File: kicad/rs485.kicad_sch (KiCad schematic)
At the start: 12 parts

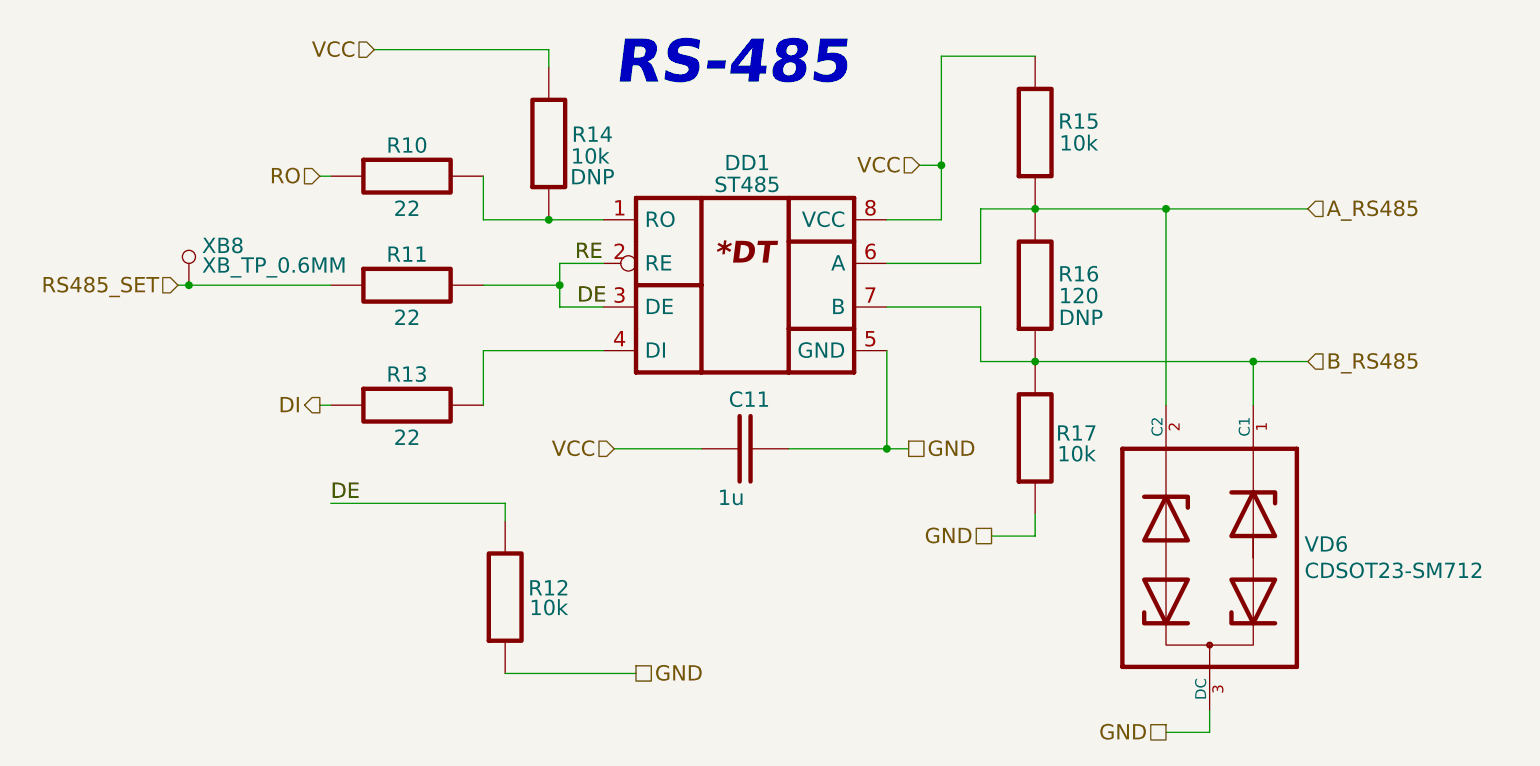
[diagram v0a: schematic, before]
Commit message: Reannotate schematic; Fix 5032 crystal footprint field; Update PCB with 5032 crystal
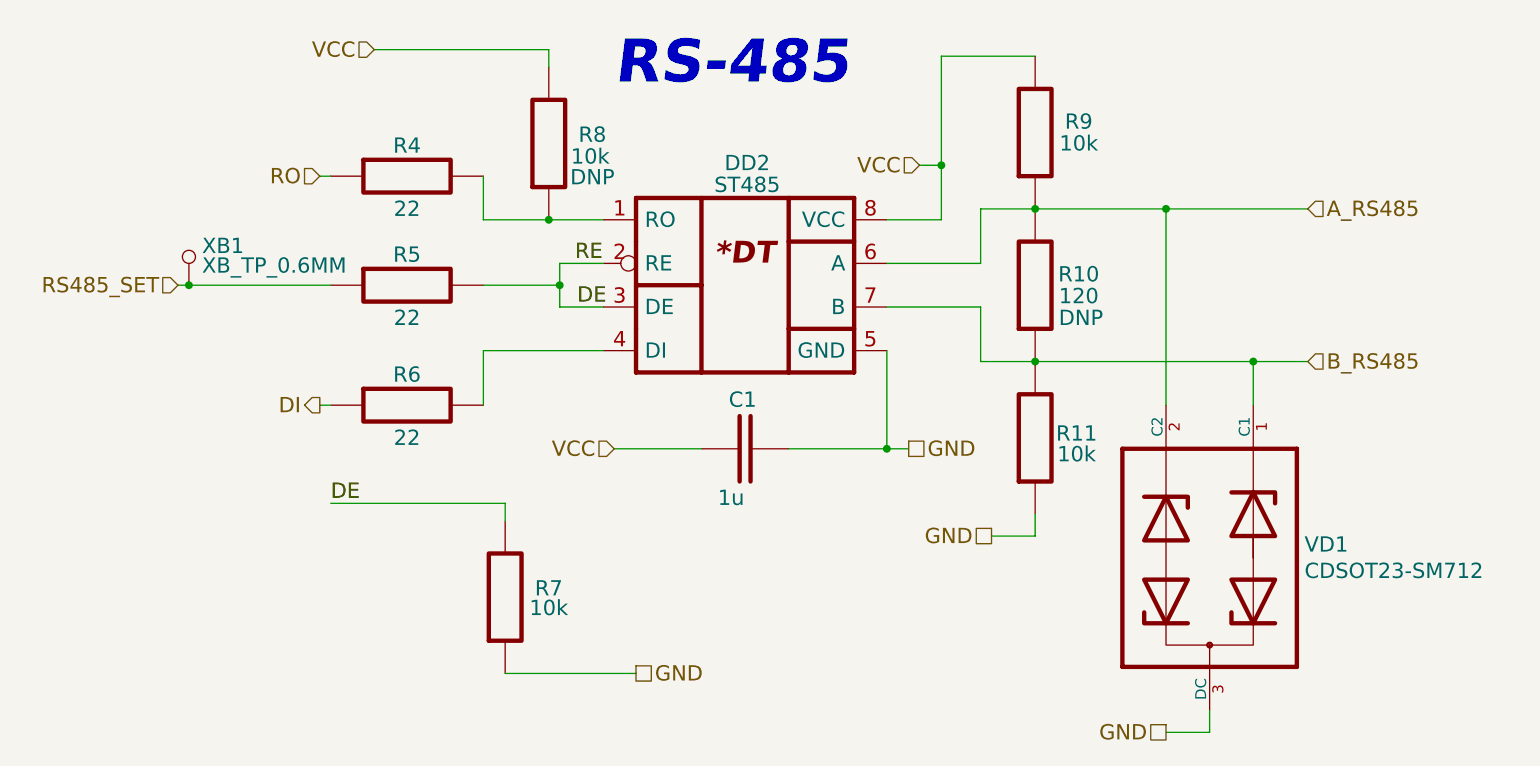
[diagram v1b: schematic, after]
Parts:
- renumbered C11 to C1, DD1 to DD2, R16 to R10, R17 to R11, R10 to R4, R11 to R5, R13 to R6, R12 to R7, R14 to R8, R15 to R9, VD6 to VD1, XB8 to XB1
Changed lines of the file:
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@@
   (symbol (lib_id "Resistors:R_RES") (at 179.578 86.36 90) (unit 1)
     (in_bom yes) (on_board yes)
-    (property "Reference" "R16" (id 0) (at 184.658 85.09 90)
+    (property "Reference" "R10" (id 0) (at 184.658 85.09 90)
       (effects (font (size 1.778 1.778)))
     )
@@
   (symbol (lib_id "Diodes:VD_TVS_ARRAY4") (at 204.978 118.11 270) (unit 1)
     (in_bom yes) (on_board yes)
-    (property "Reference" "VD6" (id 0) (at 210.947 116.5606 90)
+    (property "Reference" "VD1" (id 0) (at 210.947 116.5606 90)
       (effects (font (size 1.778 1.778)) (justify left))
     )
@@
   (symbol (lib_id "Capacitors:C_CAP") (at 145.796 105.41 0) (unit 1)
     (in_bom yes) (on_board yes)
-    (property "Reference" "C11" (id 0) (at 143.891 99.695 0)
+    (property "Reference" "C1" (id 0) (at 143.891 99.695 0)
       (effects (font (size 1.778 1.778)) (justify left))
     )
@@
   (symbol (lib_id "Chips:ST485") (at 145.796 86.36 0) (unit 1)
     (in_bom yes) (on_board yes)
-    (property "Reference" "DD1" (id 0) (at 146.05 72.136 0)
+    (property "Reference" "DD2" (id 0) (at 146.05 72.136 0)
       (effects (font (size 1.778 1.778)))
     )
@@
   (symbol (lib_id "Resistors:R_RES") (at 106.426 86.36 0) (unit 1)
     (in_bom yes) (on_board yes)
-    (property "Reference" "R11" (id 0) (at 106.426 82.804 0)
+    (property "Reference" "R5" (id 0) (at 106.426 82.804 0)
       (effects (font (size 1.778 1.778)))
     )
@@
   (symbol (lib_id "Resistors:R_RES") (at 106.426 73.66 0) (unit 1)
     (in_bom yes) (on_board yes)
-    (property "Reference" "R10" (id 0) (at 106.426 70.104 0)
+    (property "Reference" "R4" (id 0) (at 106.426 70.104 0)
       (effects (font (size 1.778 1.778)))
     )
@@
   (symbol (lib_id "Resistors:R_RES") (at 179.578 104.14 90) (unit 1)
     (in_bom yes) (on_board yes)
-    (property "Reference" "R17" (id 0) (at 184.404 103.632 90)
+    (property "Reference" "R11" (id 0) (at 184.404 103.632 90)
       (effects (font (size 1.778 1.778)))
     )
@@
   (symbol (lib_id "Resistors:R_RES") (at 122.936 69.85 90) (unit 1)
     (in_bom yes) (on_board yes)
-    (property "Reference" "R14" (id 0) (at 128.016 68.834 90)
+    (property "Reference" "R8" (id 0) (at 128.016 68.834 90)
       (effects (font (size 1.778 1.778)))
     )
@@
   (symbol (lib_id "Resistors:R_RES") (at 106.426 100.33 0) (unit 1)
     (in_bom yes) (on_board yes)
-    (property "Reference" "R13" (id 0) (at 106.426 96.774 0)
+    (property "Reference" "R6" (id 0) (at 106.426 96.774 0)
       (effects (font (size 1.778 1.778)))
     )
@@
   (symbol (lib_id "Resistors:R_RES") (at 117.856 122.6819 90) (unit 1)
     (in_bom yes) (on_board yes)
-    (property "Reference" "R12" (id 0) (at 122.936 121.6659 90)
+    (property "Reference" "R7" (id 0) (at 122.936 121.6659 90)
       (effects (font (size 1.778 1.778)))
     )
@@
   (symbol (lib_id "Connectors:XB_TP_0.6MM") (at 81.026 86.36 0) (unit 1)
     (in_bom no) (on_board yes)
-    (property "Reference" "XB8" (id 0) (at 82.55 81.788 0)
+    (property "Reference" "XB1" (id 0) (at 82.55 81.788 0)
       (effects (font (size 1.778 1.778)) (justify left))
     )
@@
   (symbol (lib_id "Resistors:R_RES") (at 179.578 68.58 90) (unit 1)
     (in_bom yes) (on_board yes)
-    (property "Reference" "R15" (id 0) (at 184.658 67.31 90)
-      (effects (font (size 1.778 1.778)))
-    )
+    (property "Reference" "R9" (id 0) (at 184.658 67.31 90)
+      (effects (font (size 1.778 1.778)))
+    )

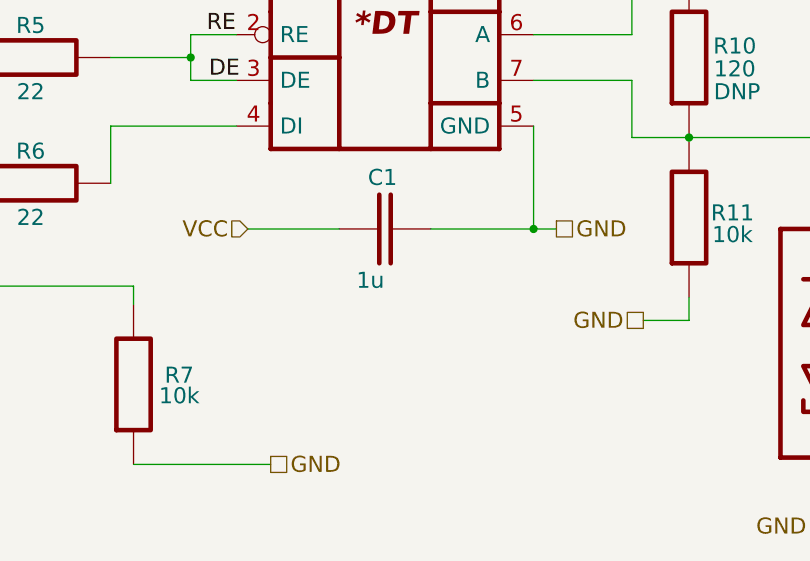
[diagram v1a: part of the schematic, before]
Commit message: Add voltage value to caps, update BOM, SCH, ASM
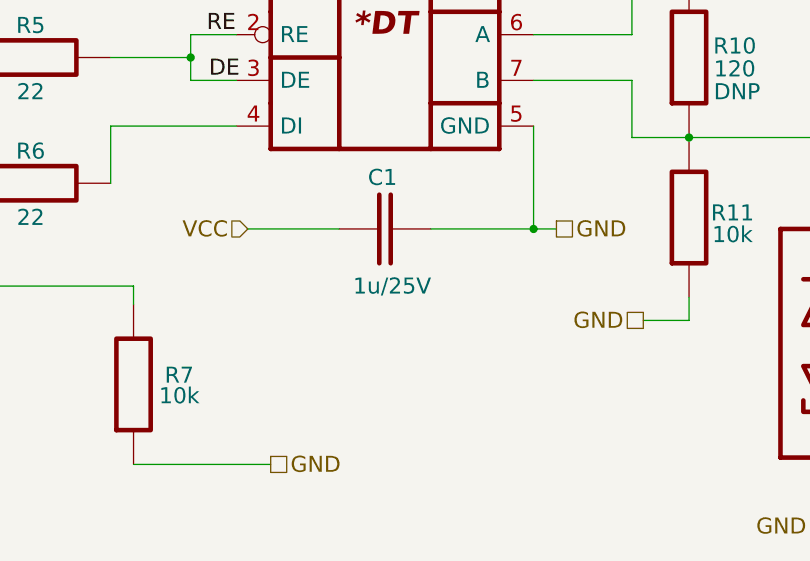
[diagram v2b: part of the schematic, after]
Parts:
- C1: value 1u -> 1u/25V; Tolerance (none) -> ±10%; Type (none) -> X7R
- R10, R11, R4, R5, R6, R7, R8, R9: Case/Package 0000 -> 0603; Tolerance ±% -> ±5%
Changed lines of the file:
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@@
     (effects (font (size 1.778 1.778)) (justify right))
   )
-  (symbol (lib_id "Resistors:R_RES") (at 179.578 86.36 90) (unit 1)
+  (symbol (lib_name "R_RES_7") (lib_id "Resistors:R_RES") (at 179.578 86.36 90) (unit 1)
     (in_bom yes) (on_board yes)
     (property "Reference" "R10" (id 0) (at 184.658 85.09 90)
@@
       (effects (font (size 1.778 1.778)))
     )
-    (property "Case/Package" "0000" (id 5) (at 185.928 86.36 0)
+    (property "Case/Package" "0603" (id 5) (at 185.928 86.36 0)
       (effects (font (size 1.27 1.27)) hide)
     )
@@
       (effects (font (size 1.27 1.27)) hide)
     )
-    (property "Tolerance" "±%" (id 7) (at 189.23 86.36 0)
-      (effects (font (size 1.27 1.27)) hide)
-    )
+    (property "Tolerance" "±5%" (id 7) (at 189.23 86.36 0)
+      (effects (font (size 1.27 1.27)) hide)
+    )
+    (property "Part Number" "" (id 8) (at 179.578 86.36 0))
     (pin "1")
     (pin "2")
@@
       (effects (font (size 1.778 1.778)) (justify left))
     )
-    (property "Value" " 1u" (id 1) (at 142.621 111.125 0)
+    (property "Value" "1u/25V" (id 1) (at 142.24 111.76 0)
       (effects (font (size 1.778 1.778)) (justify left))
     )
@@
     (property "Assembly" "" (id 4) (at 145.796 114.3 0)
       (effects (font (size 1.778 1.778)))
+    )
+    (property "Voltage" "" (id 5) (at 145.796 105.41 0)
+      (effects (font (size 1.27 1.27)) hide)
+    )
+    (property "Case/Package" "" (id 6) (at 145.796 105.41 0)
+      (effects (font (size 1.27 1.27)) hide)
+    )
+    (property "Type" "X7R" (id 7) (at 145.796 115.57 0)
+      (effects (font (size 1.27 1.27)) hide)
+    )
+    (property "Tolerance" "±10%" (id 8) (at 145.796 118.11 0)
+      (effects (font (size 1.27 1.27)) hide)
     )
     (pin "1")
@@
     (pin "8")
   )
-  (symbol (lib_id "Resistors:R_RES") (at 106.426 86.36 0) (unit 1)
+  (symbol (lib_name "R_RES_2") (lib_id "Resistors:R_RES") (at 106.426 86.36 0) (unit 1)
     (in_bom yes) (on_board yes)
     (property "Reference" "R5" (id 0) (at 106.426 82.804 0)
@@
       (effects (font (size 1.778 1.778)))
     )
-    (property "Case/Package" "0000" (id 5) (at 106.426 92.71 0)
+    (property "Case/Package" "0603" (id 5) (at 106.426 92.71 0)
       (effects (font (size 1.27 1.27)) hide)
     )
@@
       (effects (font (size 1.27 1.27)) hide)
     )
-    (property "Tolerance" "±%" (id 7) (at 106.426 96.012 0)
-      (effects (font (size 1.27 1.27)) hide)
-    )
-    (pin "1")
-    (pin "2")
-  )
-  (symbol (lib_id "Resistors:R_RES") (at 106.426 73.66 0) (unit 1)
+    (property "Tolerance" "±5%" (id 7) (at 106.426 96.012 0)
+      (effects (font (size 1.27 1.27)) hide)
+    )
+    (property "Part Number" "" (id 8) (at 106.426 86.36 0))
+    (pin "1")
+    (pin "2")
+  )
+  (symbol (lib_name "R_RES_4") (lib_id "Resistors:R_RES") (at 106.426 73.66 0) (unit 1)
     (in_bom yes) (on_board yes)
     (property "Reference" "R4" (id 0) (at 106.426 70.104 0)
@@
       (effects (font (size 1.778 1.778)))
     )
-    (property "Case/Package" "0000" (id 5) (at 106.426 80.01 0)
+    (property "Case/Package" "0603" (id 5) (at 106.426 80.01 0)
       (effects (font (size 1.27 1.27)) hide)
     )
@@
       (effects (font (size 1.27 1.27)) hide)
     )
-    (property "Tolerance" "±%" (id 7) (at 106.426 83.312 0)
-      (effects (font (size 1.27 1.27)) hide)
-    )
-    (pin "1")
-    (pin "2")
-  )
-  (symbol (lib_id "Resistors:R_RES") (at 179.578 104.14 90) (unit 1)
+    (property "Tolerance" "±5%" (id 7) (at 106.426 83.312 0)
+      (effects (font (size 1.27 1.27)) hide)
+    )
+    (property "Part Number" "" (id 8) (at 106.426 73.66 0))
+    (pin "1")
+    (pin "2")
+  )
+  (symbol (lib_name "R_RES_6") (lib_id "Resistors:R_RES") (at 179.578 104.14 90) (unit 1)
     (in_bom yes) (on_board yes)
     (property "Reference" "R11" (id 0) (at 184.404 103.632 90)
@@
       (effects (font (size 1.778 1.778)))
     )
-    (property "Case/Package" "0000" (id 5) (at 185.928 104.14 0)
+    (property "Case/Package" "0603" (id 5) (at 185.928 104.14 0)
       (effects (font (size 1.27 1.27)) hide)
     )
@@
       (effects (font (size 1.27 1.27)) hide)
     )
-    (property "Tolerance" "±%" (id 7) (at 189.23 104.14 0)
-      (effects (font (size 1.27 1.27)) hide)
-    )
-    (pin "1")
-    (pin "2")
-  )
-  (symbol (lib_id "Resistors:R_RES") (at 122.936 69.85 90) (unit 1)
+    (property "Tolerance" "±5%" (id 7) (at 189.23 104.14 0)
+      (effects (font (size 1.27 1.27)) hide)
+    )
+    (property "Part Number" "" (id 8) (at 179.578 104.14 0))
+    (pin "1")
+    (pin "2")
+  )
+  (symbol (lib_name "R_RES_5") (lib_id "Resistors:R_RES") (at 122.936 69.85 90) (unit 1)
     (in_bom yes) (on_board yes)
     (property "Reference" "R8" (id 0) (at 128.016 68.834 90)
@@
       (effects (font (size 1.778 1.778)))
     )
-    (property "Case/Package" "0000" (id 5) (at 129.286 69.85 0)
+    (property "Case/Package" "0603" (id 5) (at 129.286 69.85 0)
       (effects (font (size 1.27 1.27)) hide)
     )
@@
       (effects (font (size 1.27 1.27)) hide)
     )
-    (property "Tolerance" "±%" (id 7) (at 132.588 69.85 0)
-      (effects (font (size 1.27 1.27)) hide)
-    )
-    (pin "1")
-    (pin "2")
-  )
-  (symbol (lib_id "Resistors:R_RES") (at 106.426 100.33 0) (unit 1)
+    (property "Tolerance" "±5%" (id 7) (at 132.588 69.85 0)
+      (effects (font (size 1.27 1.27)) hide)
+    )
+    (property "Part Number" "" (id 8) (at 122.936 69.85 0))
+    (pin "1")
+    (pin "2")
+  )
+  (symbol (lib_name "R_RES_1") (lib_id "Resistors:R_RES") (at 106.426 100.33 0) (unit 1)
     (in_bom yes) (on_board yes)
     (property "Reference" "R6" (id 0) (at 106.426 96.774 0)
@@
       (effects (font (size 1.778 1.778)))
     )
-    (property "Case/Package" "0000" (id 5) (at 106.426 106.68 0)
+    (property "Case/Package" "0603" (id 5) (at 106.426 106.68 0)
       (effects (font (size 1.27 1.27)) hide)
     )
@@
       (effects (font (size 1.27 1.27)) hide)
     )
-    (property "Tolerance" "±%" (id 7) (at 106.426 109.982 0)
-      (effects (font (size 1.27 1.27)) hide)
-    )
-    (pin "1")
-    (pin "2")
-  )
-  (symbol (lib_id "Resistors:R_RES") (at 117.856 122.6819 90) (unit 1)
+    (property "Tolerance" "±5%" (id 7) (at 106.426 109.982 0)
+      (effects (font (size 1.27 1.27)) hide)
+    )
+    (property "Part Number" "" (id 8) (at 106.426 100.33 0))
+    (pin "1")
+    (pin "2")
+  )
+  (symbol (lib_name "R_RES_3") (lib_id "Resistors:R_RES") (at 117.856 122.6819 90) (unit 1)
     (in_bom yes) (on_board yes)
     (property "Reference" "R7" (id 0) (at 122.936 121.6659 90)
@@
       (effects (font (size 1.778 1.778)))
     )
-    (property "Case/Package" "0000" (id 5) (at 124.206 122.6819 0)
+    (property "Case/Package" "0603" (id 5) (at 124.206 122.6819 0)
       (effects (font (size 1.27 1.27)) hide)
     )
@@
       (effects (font (size 1.27 1.27)) hide)
     )
-    (property "Tolerance" "±%" (id 7) (at 127.508 122.6819 0)
-      (effects (font (size 1.27 1.27)) hide)
-    )
+    (property "Tolerance" "±5%" (id 7) (at 127.508 122.6819 0)
+      (effects (font (size 1.27 1.27)) hide)
+    )
+    (property "Part Number" "" (id 8) (at 117.856 122.6819 0))
     (pin "1")
     (pin "2")
@@
       (effects (font (size 1.778 1.778)))
     )
-    (property "Case/Package" "0000" (id 5) (at 185.928 68.58 0)
+    (property "Case/Package" "0603" (id 5) (at 185.928 68.58 0)
       (effects (font (size 1.27 1.27)) hide)
     )
@@
       (effects (font (size 1.27 1.27)) hide)
     )
-    (property "Tolerance" "±%" (id 7) (at 189.23 68.58 0)
-      (effects (font (size 1.27 1.27)) hide)
-    )
-    (pin "1")
-    (pin "2")
+    (property "Tolerance" "±5%" (id 7) (at 189.23 68.58 0)
+      (effects (font (size 1.27 1.27)) hide)
+    )
+    (property "Part Number" "" (id 8) (at 179.578 68.58 0))
+    (pin "1")
+    (pin "2")

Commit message: Add wiring diagram; Add work ours (stage 2); refactor folders
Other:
- title: (none) -> RadioSens v1
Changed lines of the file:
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@@
 (kicad_sch (version 20211123) (generator eeschema)
   (paper "A4")
+  (title_block
+    (title "RadioSens v1")
+    (comment 2 "Electrical Circuit")
+  )
   (junction (at 204.978 95.25) (diameter 0) (color 0 0 0 0)
   )
